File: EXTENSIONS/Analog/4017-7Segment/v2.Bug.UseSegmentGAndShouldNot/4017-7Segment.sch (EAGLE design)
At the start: 7 parts

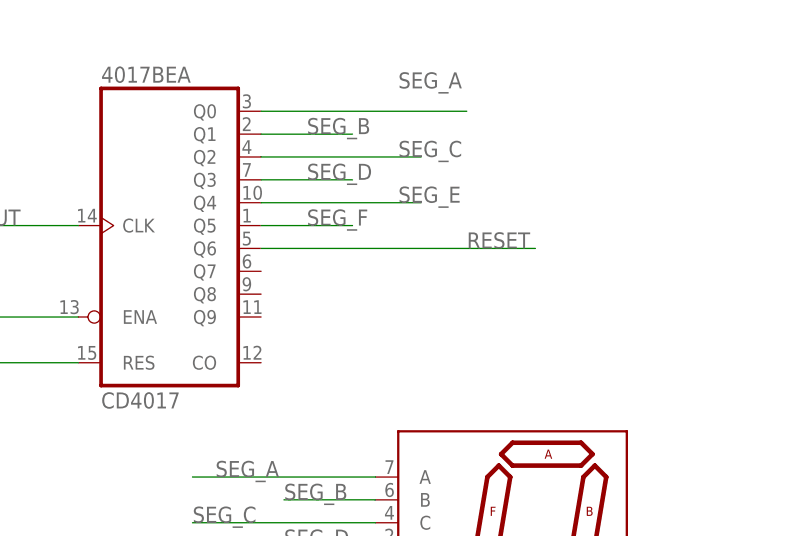
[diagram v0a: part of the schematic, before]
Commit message: Fix bug in 4017-7Segment v2
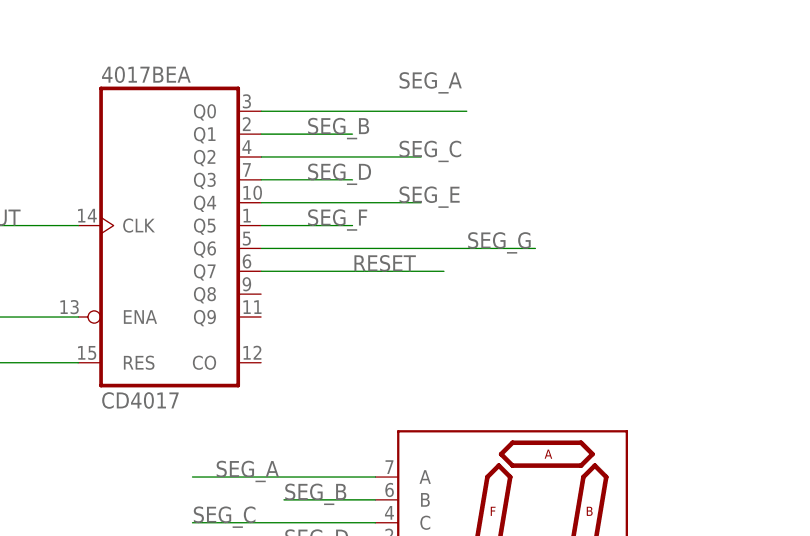
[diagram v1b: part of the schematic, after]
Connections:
- net RESET: now also 4017BEA.Q7; no longer 4017BEA.Q6
- net SEG_G: now also 4017BEA.Q6
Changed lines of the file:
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@@
 <label x="-68.58" y="66.04" size="1.778" layer="95"/>
+</segment>
+<segment>
+<pinref part="4017BE" gate="A" pin="Q6"/>
+<wire x1="-60.96" y1="106.68" x2="-30.48" y2="106.68" width="0.1524" layer="91"/>
+<label x="-38.1" y="106.68" size="1.778" layer="95"/>
 </segment>
 </net>
@@
 <net name="RESET" class="0">
 <segment>
+<pinref part="4017BE" gate="A" pin="Q7"/>
+<wire x1="-60.96" y1="104.14" x2="-40.64" y2="104.14" width="0.1524" layer="91"/>
+<label x="-50.8" y="104.14" size="1.778" layer="95"/>
+</segment>
+<segment>
 <pinref part="4017BE" gate="A" pin="RES"/>
 <wire x1="-81.28" y1="93.98" x2="-99.06" y2="93.98" width="0.1524" layer="91"/>
 <label x="-99.06" y="93.98" size="1.778" layer="95"/>
 </segment>
-<segment>
-<pinref part="4017BE" gate="A" pin="Q6"/>
-<wire x1="-60.96" y1="106.68" x2="-30.48" y2="106.68" width="0.1524" layer="91"/>
-<label x="-38.1" y="106.68" size="1.778" layer="95"/>
-</segment>
 </net>
